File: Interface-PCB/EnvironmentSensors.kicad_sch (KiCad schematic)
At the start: 37 parts, among them IC1 SN74LVC245AN, J10 LEVEL_SENSOR, J11 LEVEL_SENSOR, J12 TEMPERATURE_SENSOR, J13 TEMPERATURE_SENSOR, J6 LEVEL_SENSOR, J7 LEVEL_SENSOR, J8 LEVEL_SENSOR, J9 LEVEL_SENSOR

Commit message: Add JST Connector Footprints
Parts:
- C1: footprint Capacitor_THT:C_Disc_D3.4mm_W2.1mm_P2.50mm -> AA_Custom_Components:C_Ceramic_Disc_D4.3mm_W1.9mm_P5.08mm
- J10, J11, J12, J13, J6, J7, J8, J9: footprint Connector_JST:JST_XH_B3B-XH-A_1x03_P2.50mm_Vertical -> AA_Custom_Components:JST_XH_1x03_P2.54mm_Vertical
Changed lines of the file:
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@@
       (effects (font (size 1.143 1.143)) (justify right))
     )
-    (property "Footprint" "Connector_JST:JST_XH_B3B-XH-A_1x03_P2.50mm_Vertical" (id 2) (at 86.36 29.21 0)
+    (property "Footprint" "AA_Custom_Components:JST_XH_1x03_P2.54mm_Vertical" (id 2) (at 86.36 29.21 0)
       (effects (font (size 0.508 0.508)) hide)
     )
@@
       (effects (font (size 1.143 1.143)) (justify right))
     )
-    (property "Footprint" "Connector_JST:JST_XH_B3B-XH-A_1x03_P2.50mm_Vertical" (id 2) (at 86.36 50.8 0)
+    (property "Footprint" "AA_Custom_Components:JST_XH_1x03_P2.54mm_Vertical" (id 2) (at 86.36 50.8 0)
       (effects (font (size 0.508 0.508)) hide)
     )
@@
       (effects (font (size 1.143 1.143)) (justify right))
     )
-    (property "Footprint" "Connector_JST:JST_XH_B3B-XH-A_1x03_P2.50mm_Vertical" (id 2) (at 38.1 50.8 0)
+    (property "Footprint" "AA_Custom_Components:JST_XH_1x03_P2.54mm_Vertical" (id 2) (at 38.1 50.8 0)
       (effects (font (size 0.508 0.508)) hide)
     )
@@
       (effects (font (size 1.143 1.143)) (justify right))
     )
-    (property "Footprint" "Connector_JST:JST_XH_B3B-XH-A_1x03_P2.50mm_Vertical" (id 2) (at 38.1 29.21 0)
+    (property "Footprint" "AA_Custom_Components:JST_XH_1x03_P2.54mm_Vertical" (id 2) (at 38.1 29.21 0)
       (effects (font (size 0.508 0.508)) hide)
     )
@@
       (effects (font (size 1.143 1.143)) (justify right))
     )
-    (property "Footprint" "Connector_JST:JST_XH_B3B-XH-A_1x03_P2.50mm_Vertical" (id 2) (at 151.13 111.76 0)
+    (property "Footprint" "AA_Custom_Components:JST_XH_1x03_P2.54mm_Vertical" (id 2) (at 151.13 111.76 0)
       (effects (font (size 0.508 0.508)) hide)
     )
@@
       (effects (font (size 1.143 1.143)) (justify right))
     )
-    (property "Footprint" "Connector_JST:JST_XH_B3B-XH-A_1x03_P2.50mm_Vertical" (id 2) (at 151.13 86.36 0)
+    (property "Footprint" "AA_Custom_Components:JST_XH_1x03_P2.54mm_Vertical" (id 2) (at 151.13 86.36 0)
       (effects (font (size 0.508 0.508)) hide)
     )
@@
       (effects (font (size 1.143 1.143)) (justify right))
     )
-    (property "Footprint" "Connector_JST:JST_XH_B3B-XH-A_1x03_P2.50mm_Vertical" (id 2) (at 86.36 72.39 0)
+    (property "Footprint" "AA_Custom_Components:JST_XH_1x03_P2.54mm_Vertical" (id 2) (at 86.36 72.39 0)
       (effects (font (size 0.508 0.508)) hide)
     )
@@
       (effects (font (size 1.143 1.143)) (justify right))
     )
-    (property "Footprint" "Connector_JST:JST_XH_B3B-XH-A_1x03_P2.50mm_Vertical" (id 2) (at 38.1 72.39 0)
+    (property "Footprint" "AA_Custom_Components:JST_XH_1x03_P2.54mm_Vertical" (id 2) (at 38.1 72.39 0)
       (effects (font (size 0.508 0.508)) hide)
     )
@@
       (effects (font (size 1.27 1.27)) (justify left))
     )
-    (property "Footprint" "Capacitor_THT:C_Disc_D3.4mm_W2.1mm_P2.50mm" (id 2) (at 194.0052 30.48 0)
-      (effects (font (size 1.27 1.27)) hide)
-    )
+    (property "Footprint" "AA_Custom_Components:C_Ceramic_Disc_D4.3mm_W1.9mm_P5.08mm" (id 2) (at 194.0052 30.48 0)
+      (effects (font (size 1.27 1.27)) hide)
+    )

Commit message: Update Header pin and Buzzer Footprints
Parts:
- BZ1: footprint Buzzer_Beeper:Buzzer_TDK_PS1240P02BT_D12.2mm_H6.5mm -> AA_Custom_Components:Buzzer_Generic_D12.2mm_H6.5mm
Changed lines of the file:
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@@
       (effects (font (size 1.27 1.27)) (justify left))
     )
-    (property "Footprint" "Buzzer_Beeper:Buzzer_TDK_PS1240P02BT_D12.2mm_H6.5mm" (id 2) (at 88.265 143.51 90)
+    (property "Footprint" "AA_Custom_Components:Buzzer_Generic_D12.2mm_H6.5mm" (id 2) (at 88.265 143.51 90)
       (effects (font (size 1.27 1.27)) hide)
     )

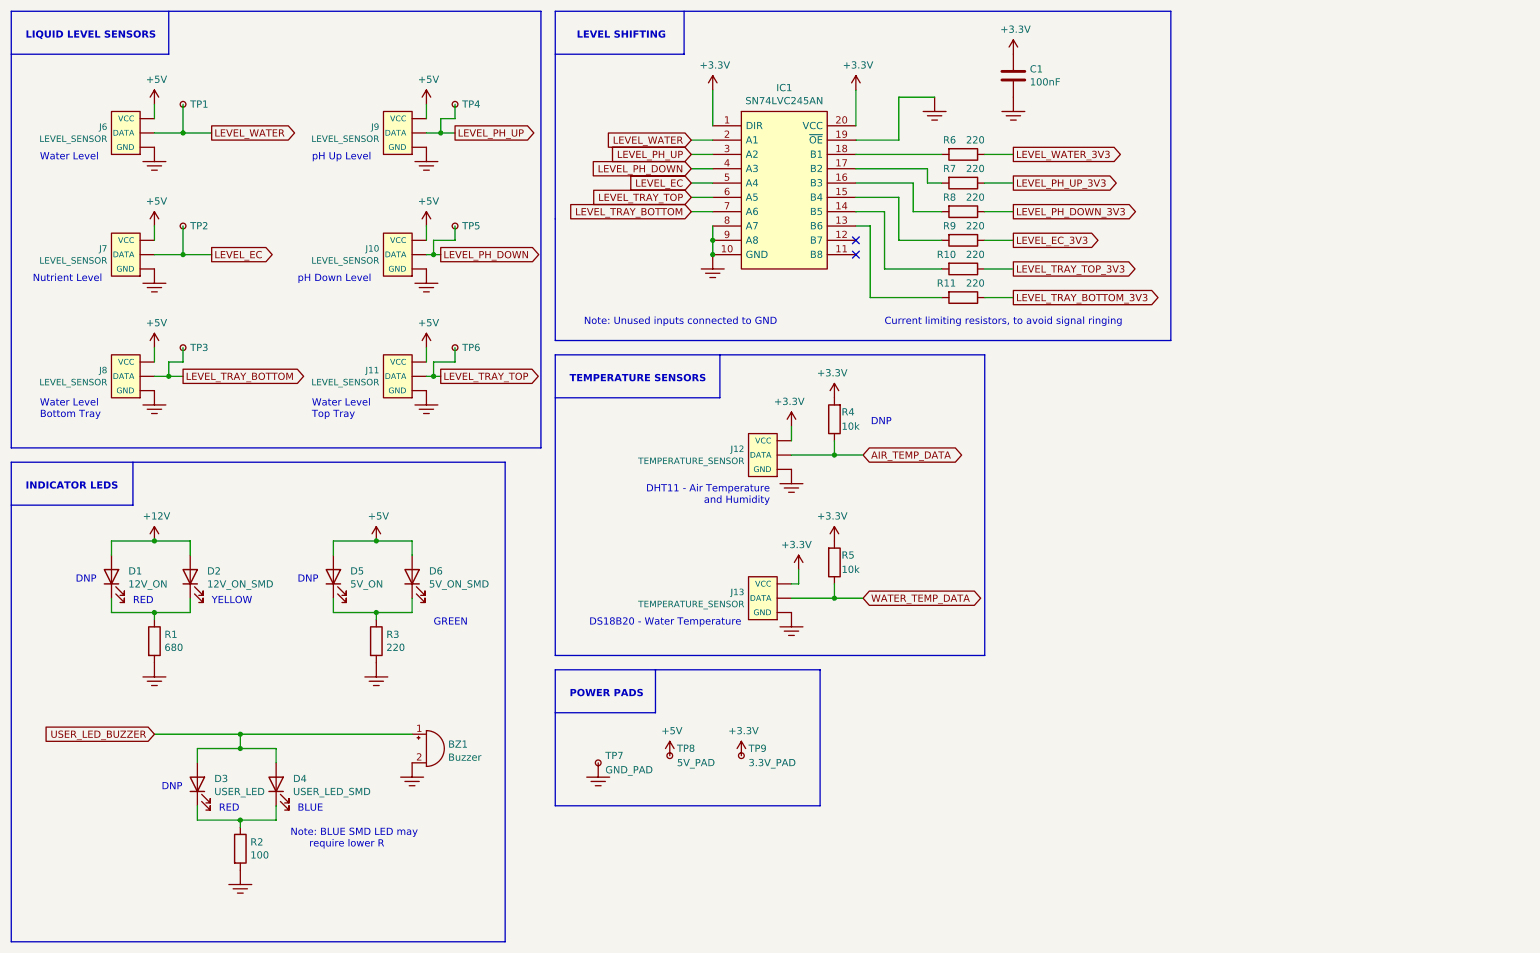
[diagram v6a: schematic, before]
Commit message: Complete Initial Layout of PCB
- aligned to 5mm grid
- 100x100mm board
- update footprints
- align 2 resistors to 2.54mm spacing
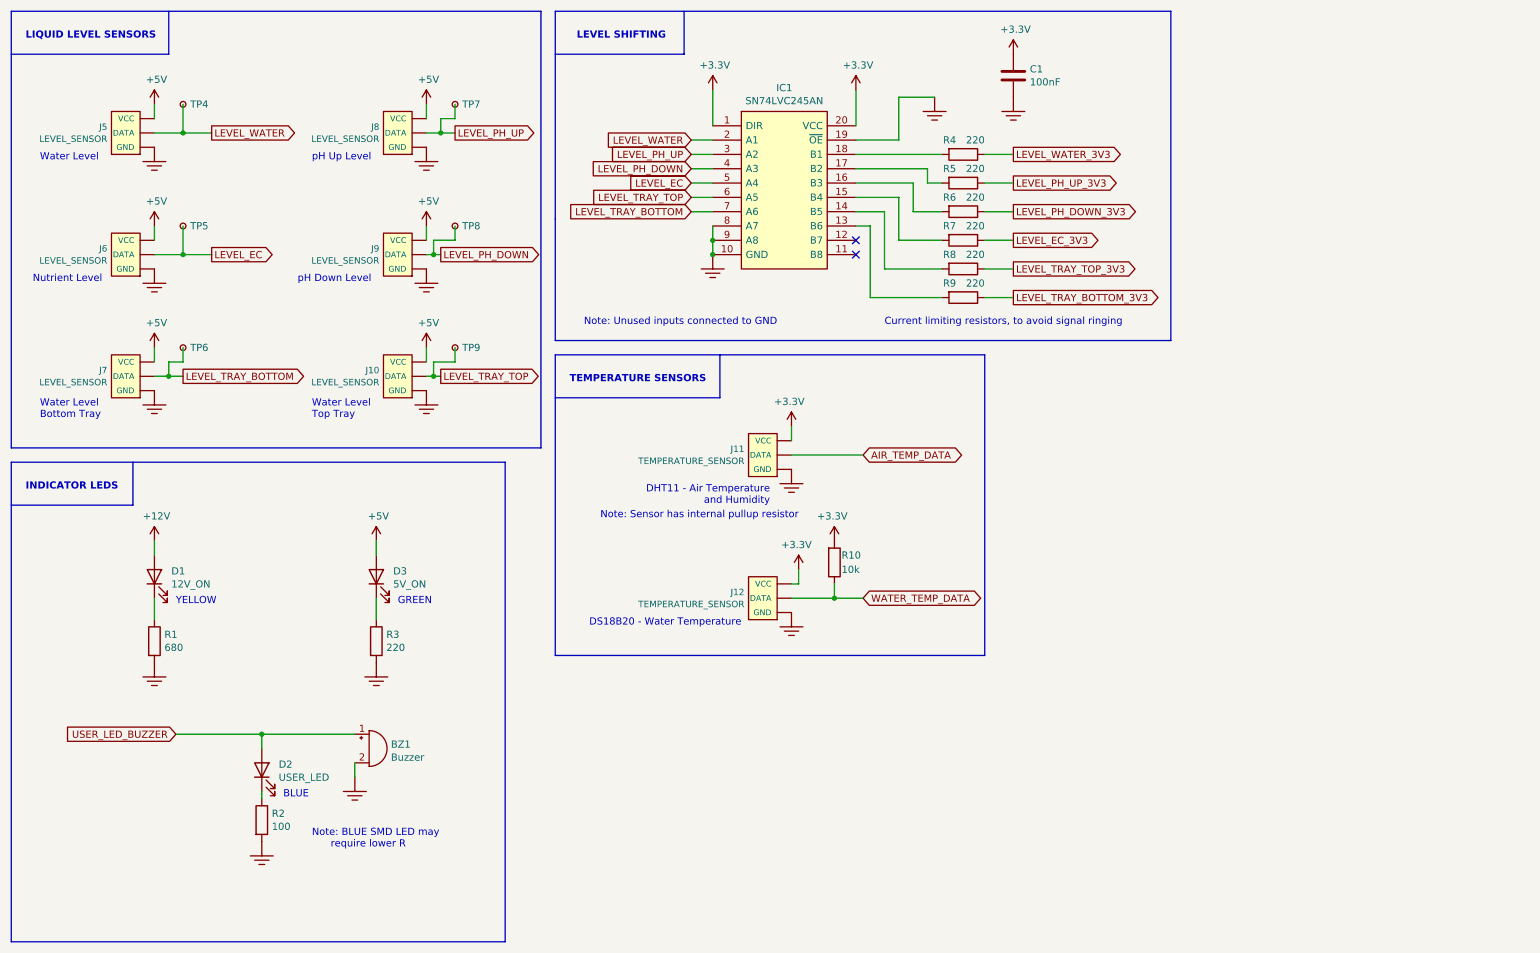
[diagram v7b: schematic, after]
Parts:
- removed D1: 12V_ON, LED_THT:LED_D3.0mm, symbol Device:LED
- removed D3: USER_LED, LED_THT:LED_D3.0mm, symbol Device:LED
- removed D5: 5V_ON, LED_THT:LED_D3.0mm, symbol Device:LED
- removed R4: 10k, AA_Custom_Components:R_SS_Axial_DIN0207_L6.3mm_D2.5mm_P10.16mm_Horizontal, symbol Device:R
- removed TP7: GND_PAD, AA_Custom_Components:TestPoint_Pad_5.0x5.0mm, symbol Connector:TestPoint_Small
- removed TP8: 5V_PAD, AA_Custom_Components:TestPoint_Pad_5.0x5.0mm, symbol Connector:TestPoint_Small
- removed TP9: 3.3V_PAD, AA_Custom_Components:TestPoint_Pad_5.0x5.0mm, symbol Connector:TestPoint_Small
- D1: renamed from D2; value 12V_ON_SMD -> 12V_ON
- D2: renamed from D4; value USER_LED_SMD -> USER_LED
- D3: renamed from D6; value 5V_ON_SMD -> 5V_ON
- renumbered J11 to J10, J12 to J11, J13 to J12, J6 to J5, J7 to J6, J8 to J7, J9 to J8, J10 to J9, R5 to R10, R6 to R4, R7 to R5, R8 to R6, R9 to R7, R10 to R8, R11 to R9, TP1 to TP4, TP2 to TP5, TP3 to TP6, TP4 to TP7, TP5 to TP8, TP6 to TP9
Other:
- note added: "Note: Sensor has internal pullup resistor"
- note removed: "DNP"
- note removed: "POWER PADS"
- note removed: "RED"
- moved on the sheet: BZ1, D1, D2, D3, R2

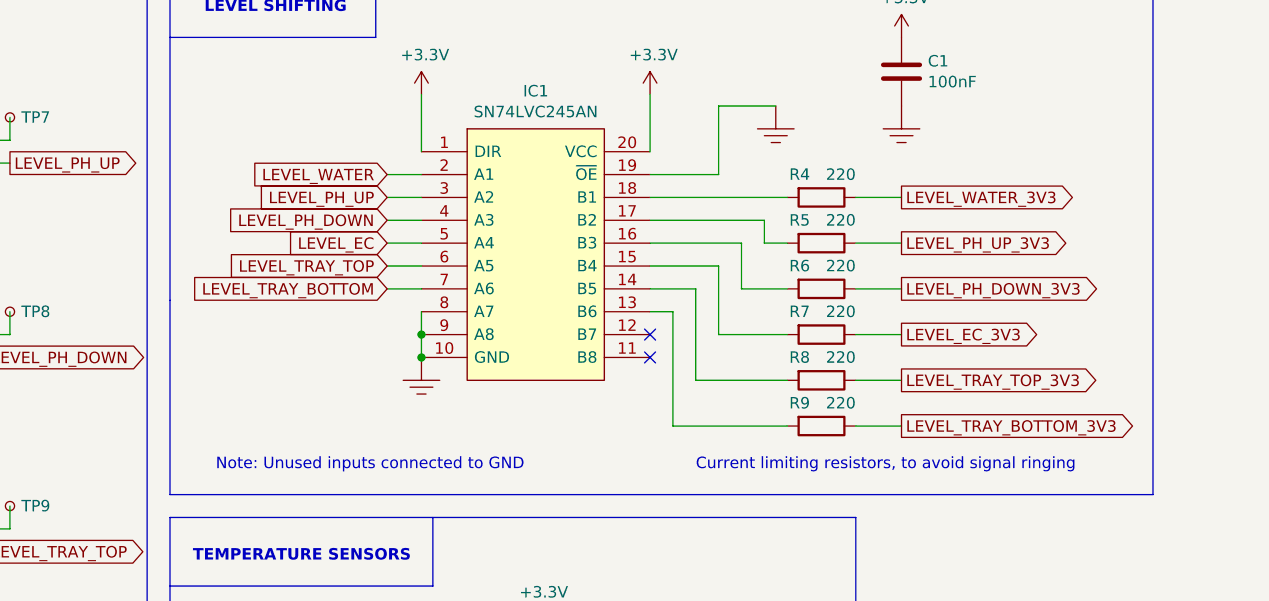
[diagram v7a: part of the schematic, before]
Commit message: Increase board size, Add connector labels
- Increase board size to 140x130mm
- Refine layout on PCB
- Align breakout board resistors to 2.54mm spacing
- Add Inverted silkscreen labels for off-board connectors
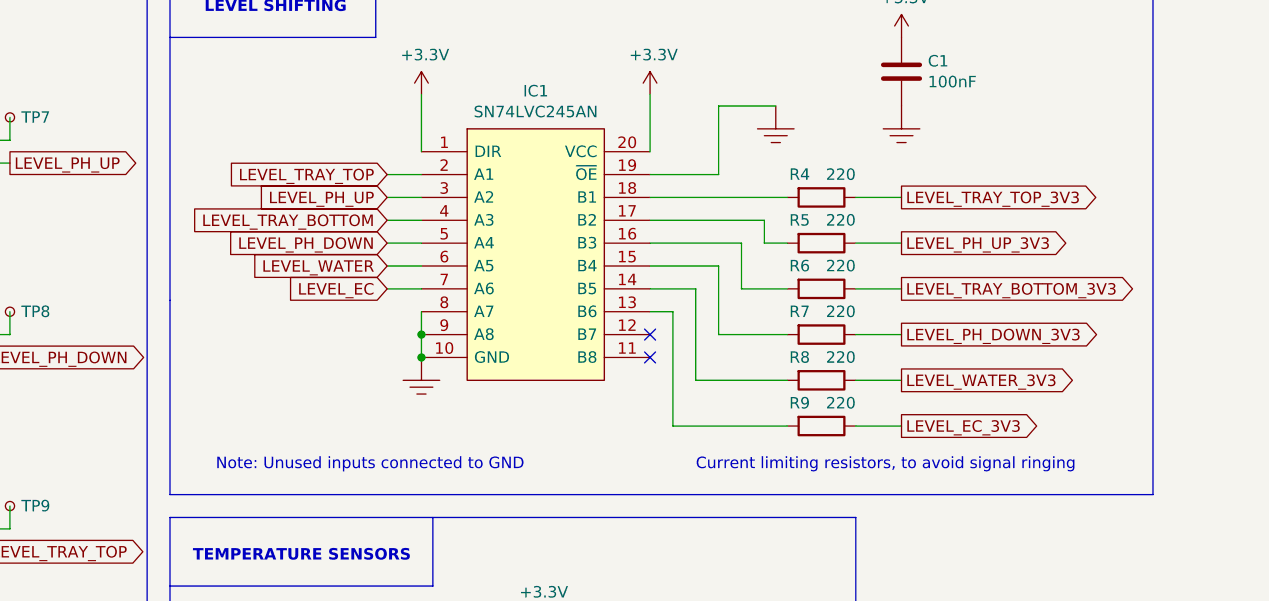
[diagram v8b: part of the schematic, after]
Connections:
- net LEVEL_EC: now also IC1.7 (A6); no longer IC1.5 (A4)
- net LEVEL_EC_3V3: now also R9.1; no longer R7.1
- net LEVEL_PH_DOWN: now also IC1.5 (A4); no longer IC1.4 (A3)
- net LEVEL_PH_DOWN_3V3: now also R7.1; no longer R6.1
- net LEVEL_TRAY_BOTTOM: now also IC1.4 (A3); no longer IC1.7 (A6)
- net LEVEL_TRAY_BOTTOM_3V3: now also R6.1; no longer R9.1
- net LEVEL_TRAY_TOP: now also IC1.2 (A1); no longer IC1.6 (A5)
- net LEVEL_TRAY_TOP_3V3: now also R4.1; no longer R8.1
- net LEVEL_WATER: now also IC1.6 (A5); no longer IC1.2 (A1)
- net LEVEL_WATER_3V3: now also R8.1; no longer R4.1
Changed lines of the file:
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@@
     )
   )
-  (global_label "LEVEL_WATER_3V3" (shape output) (at 193.04 40.64 0) (fields_autoplaced)
+  (global_label "LEVEL_WATER_3V3" (shape output) (at 193.04 60.96 0) (fields_autoplaced)
     (effects (font (size 1.27 1.27)) (justify left))
-    (property "Intersheet References" "${INTERSHEET_REFS}" (id 0) (at -46.99 -12.7 0)
+    (property "Intersheet References" "${INTERSHEET_REFS}" (id 0) (at -46.99 7.62 0)
       (effects (font (size 1.27 1.27)) hide)
     )
@@
     )
   )
-  (global_label "LEVEL_TRAY_BOTTOM_3V3" (shape output) (at 193.04 66.04 0) (fields_autoplaced)
+  (global_label "LEVEL_TRAY_BOTTOM_3V3" (shape output) (at 193.04 50.8 0) (fields_autoplaced)
     (effects (font (size 1.27 1.27)) (justify left))
-    (property "Intersheet References" "${INTERSHEET_REFS}" (id 0) (at -46.99 0 0)
+    (property "Intersheet References" "${INTERSHEET_REFS}" (id 0) (at -46.99 -15.24 0)
       (effects (font (size 1.27 1.27)) hide)
     )
@@
     )
   )
-  (global_label "LEVEL_TRAY_TOP" (shape input) (at 135.89 48.26 180) (fields_autoplaced)
+  (global_label "LEVEL_TRAY_TOP" (shape input) (at 135.89 38.1 180) (fields_autoplaced)
     (effects (font (size 1.27 1.27)) (justify right))
-    (property "Intersheet References" "${INTERSHEET_REFS}" (id 0) (at -73.66 -12.7 0)
+    (property "Intersheet References" "${INTERSHEET_REFS}" (id 0) (at -73.66 -22.86 0)
       (effects (font (size 1.27 1.27)) hide)
     )
   )
-  (global_label "LEVEL_PH_DOWN" (shape input) (at 135.89 43.18 180) (fields_autoplaced)
+  (global_label "LEVEL_PH_DOWN" (shape input) (at 135.89 45.72 180) (fields_autoplaced)
     (effects (font (size 1.27 1.27)) (justify right))
-    (property "Intersheet References" "${INTERSHEET_REFS}" (id 0) (at -73.66 -12.7 0)
+    (property "Intersheet References" "${INTERSHEET_REFS}" (id 0) (at -73.66 -10.16 0)
       (effects (font (size 1.27 1.27)) hide)
     )
@@
     )
   )
-  (global_label "LEVEL_EC_3V3" (shape output) (at 193.04 55.88 0) (fields_autoplaced)
+  (global_label "LEVEL_EC_3V3" (shape output) (at 193.04 66.04 0) (fields_autoplaced)
     (effects (font (size 1.27 1.27)) (justify left))
-    (property "Intersheet References" "${INTERSHEET_REFS}" (id 0) (at -46.99 -5.08 0)
+    (property "Intersheet References" "${INTERSHEET_REFS}" (id 0) (at -46.99 5.08 0)
       (effects (font (size 1.27 1.27)) hide)
     )
@@
     )
   )
-  (global_label "LEVEL_WATER" (shape input) (at 135.89 38.1 180) (fields_autoplaced)
+  (global_label "LEVEL_WATER" (shape input) (at 135.89 48.26 180) (fields_autoplaced)
     (effects (font (size 1.27 1.27)) (justify right))
-    (property "Intersheet References" "${INTERSHEET_REFS}" (id 0) (at -73.66 -12.7 0)
+    (property "Intersheet References" "${INTERSHEET_REFS}" (id 0) (at -73.66 -2.54 0)
       (effects (font (size 1.27 1.27)) hide)
     )
@@
     )
   )
-  (global_label "LEVEL_TRAY_BOTTOM" (shape input) (at 135.89 50.8 180) (fields_autoplaced)
+  (global_label "LEVEL_TRAY_BOTTOM" (shape input) (at 135.89 43.18 180) (fields_autoplaced)
     (effects (font (size 1.27 1.27)) (justify right))
-    (property "Intersheet References" "${INTERSHEET_REFS}" (id 0) (at -73.66 -12.7 0)
+    (property "Intersheet References" "${INTERSHEET_REFS}" (id 0) (at -73.66 -20.32 0)
       (effects (font (size 1.27 1.27)) hide)
     )
   )
-  (global_label "LEVEL_TRAY_TOP_3V3" (shape output) (at 193.04 60.96 0) (fields_autoplaced)
+  (global_label "LEVEL_TRAY_TOP_3V3" (shape output) (at 193.04 40.64 0) (fields_autoplaced)
+    (effects (font (size 1.27 1.27)) (justify left))
+    (property "Intersheet References" "${INTERSHEET_REFS}" (id 0) (at -46.99 -22.86 0)
+      (effects (font (size 1.27 1.27)) hide)
+    )
+  )
+  (global_label "LEVEL_PH_DOWN_3V3" (shape output) (at 193.04 55.88 0) (fields_autoplaced)
     (effects (font (size 1.27 1.27)) (justify left))
     (property "Intersheet References" "${INTERSHEET_REFS}" (id 0) (at -46.99 -2.54 0)
@@
     )
   )
-  (global_label "LEVEL_PH_DOWN_3V3" (shape output) (at 193.04 50.8 0) (fields_autoplaced)
-    (effects (font (size 1.27 1.27)) (justify left))
-    (property "Intersheet References" "${INTERSHEET_REFS}" (id 0) (at -46.99 -7.62 0)
+  (global_label "LEVEL_EC" (shape input) (at 135.89 50.8 180) (fields_autoplaced)
+    (effects (font (size 1.27 1.27)) (justify right))
+    (property "Intersheet References" "${INTERSHEET_REFS}" (id 0) (at -73.66 -7.62 0)
       (effects (font (size 1.27 1.27)) hide)
     )
-  )
-  (global_label "LEVEL_EC" (shape input) (at 135.89 45.72 180) (fields_autoplaced)
-    (effects (font (size 1.27 1.27)) (justify right))
-    (property "Intersheet References" "${INTERSHEET_REFS}" (id 0) (at -73.66 -12.7 0)
-      (effects (font (size 1.27 1.27)) hide)
-    )
